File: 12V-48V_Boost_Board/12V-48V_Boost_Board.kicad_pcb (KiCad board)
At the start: 2 copper layers, 31 parts, among them J1 12V Input, J2 Input Current Sensing, J3 Output Current Sensing, J4 48V Output, Q1 100V

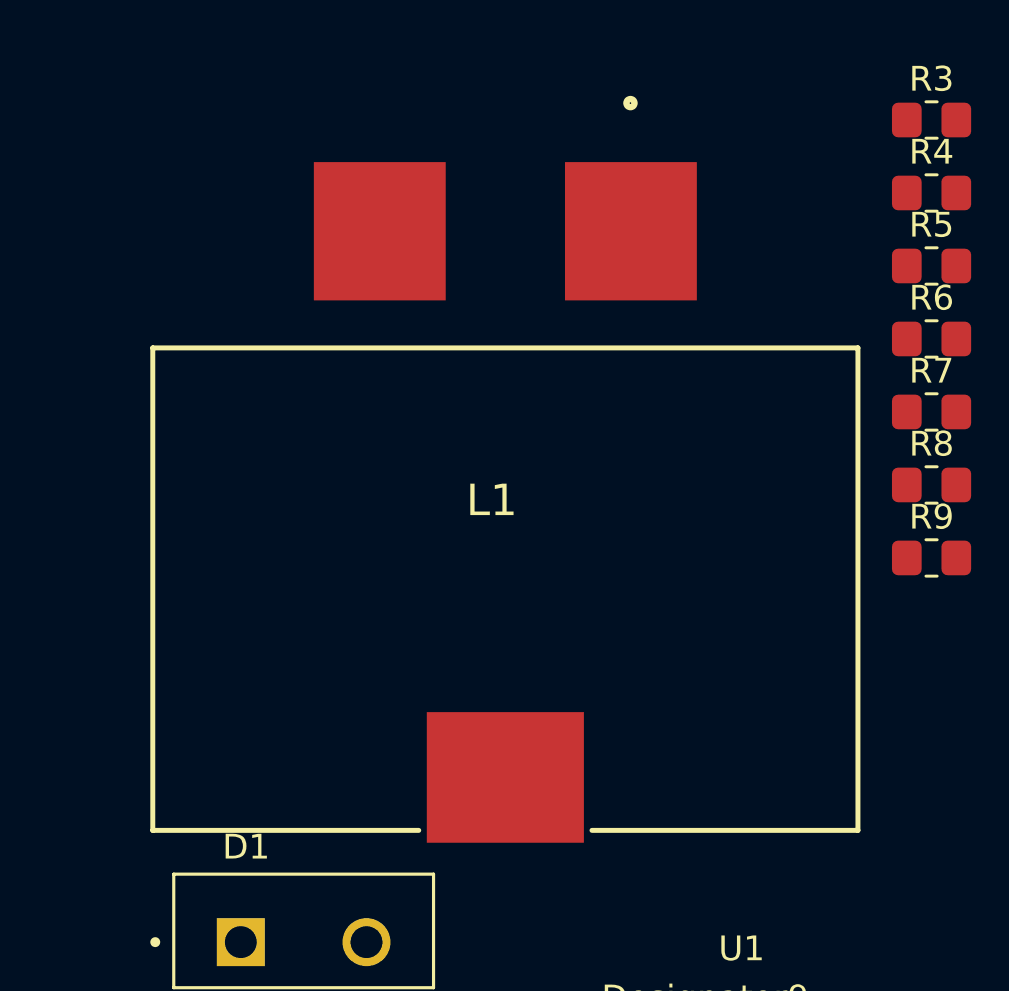
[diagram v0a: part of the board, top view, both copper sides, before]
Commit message: Implemented feedback from request V2
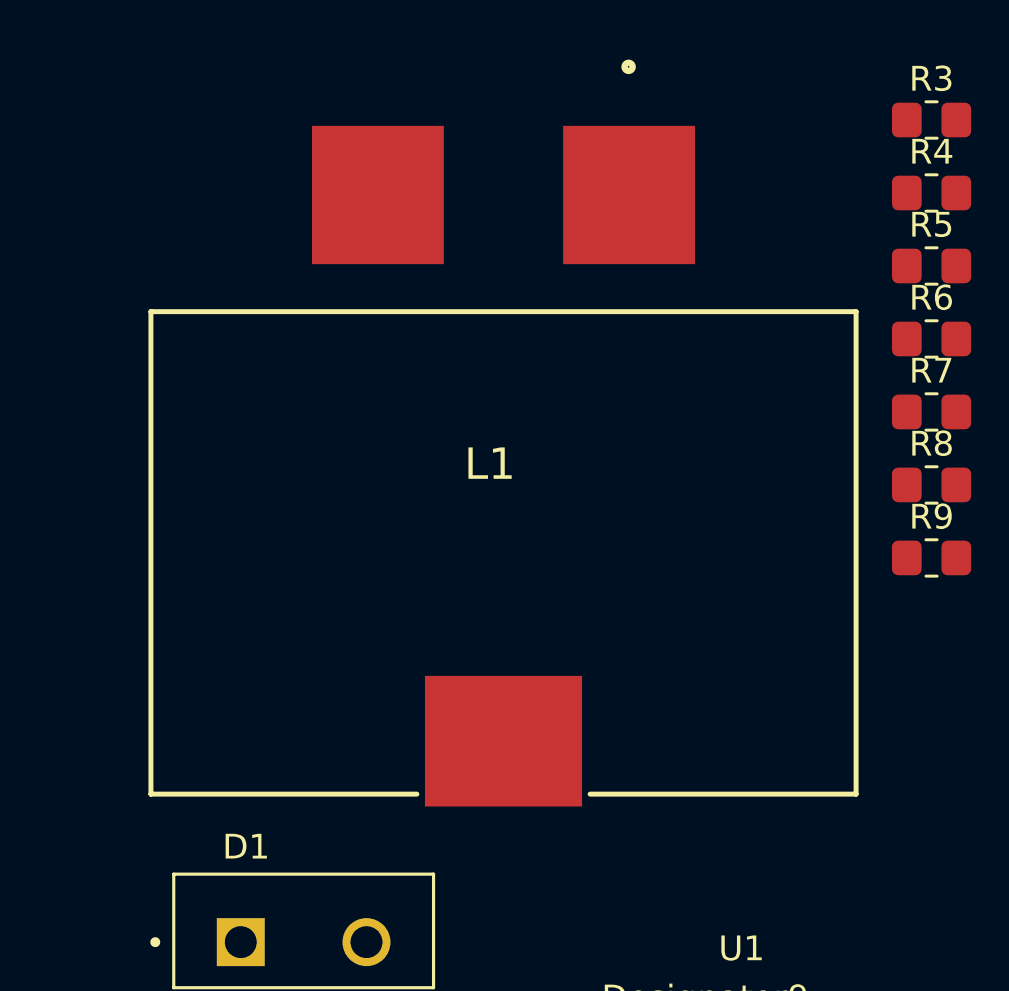
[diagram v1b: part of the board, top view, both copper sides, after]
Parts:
- moved L1 1.47 mm to (151.0, 107.0)
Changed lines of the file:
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@@
 	(footprint "Library:WE-HCF_SMD_HIGH-CURRENT_INDUCTOR"
 		(layer "F.Cu")
-		(at 151.075 108.465)
+		(at 151 107)
 		(descr "WE-HCF_SMD_High-Current_Inductor")
 		(tags "Inductor")

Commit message: First attempt in the pcb layout and routing
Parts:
- added C12: 1µF, Capacitor_SMD:C_0805_2012Metric_Pad1.18x1.45mm_HandSolder, F.Cu at (136.5, 128.0)
- added DNP1: 1mΩ, Resistor_SMD:R_0805_2012Metric_Pad1.20x1.40mm_HandSolder, F.Cu at (125.5, 100.5)
- added DNP2: ~, Resistor_SMD:R_0805_2012Metric_Pad1.20x1.40mm_HandSolder, F.Cu at (125.5, 93.5)
- added J5: Output Measuring, TerminalBlock_Phoenix:TerminalBlock_Phoenix_PT-1,5-2-5.0-H_1x02_P5.00mm_Horizontal, F.Cu at (117.0, 96.5)
- C11: value 1µF -> 10µF
- C2: value 100nF -> 4.7µF
- C3: value 63nF -> 100nF
- C4: value 1µF -> 63nF
- C5: value 120nF -> 1µF
- C6: value 100nF -> 120nF
- C7: value 1nF -> 100nF
- C8: value 10µF -> 1nF
- D1: value 800mV -> 455mV; footprint Library:TO-220-2 -> 12/48 boost:D2PAK_STM-M
- F1: footprint Fuse:Fuse_0805_2012Metric_Pad1.15x1.40mm_HandSolder -> Fuse:Fuse_1206_3216Metric
- F2: value 3A -> 2A; footprint Fuse:Fuse_0805_2012Metric_Pad1.15x1.40mm_HandSolder -> Fuse:Fuse_1206_3216Metric
- L1: footprint Library:WE-HCF_SMD_HIGH-CURRENT_INDUCTOR -> 12/48 boost:WE-HCF_SMD_HIGH-CURRENT_INDUCTOR
- Q1: value 100V -> FDWS86068-F085; footprint Library:Q1 Mosfet -> 12/48 boost:Q1 Mosfet
- TH1: footprint Library:Inrush Current Limiter -> 12/48 boost:Inrush Current Limiter
- U1: footprint Library:LM5156H -> 12/48 boost:LM5156H
- moved F1 78.4 mm to (194.0, 81.2), turned to -90 degrees
- moved J2 76.3 mm to (179.0, 78.5)
- moved TH1 66.3 mm to (187.5, 91.2), turned to -90 degrees
- moved R1 65.7 mm to (180.5, 86.0)
- moved J1 61.1 mm to (166.5, 78.5)
- moved C11 51.4 mm to (136.5, 132.0), turned to 180 degrees
- moved C10 49.4 mm to (141.5, 132.0), turned to 180 degrees
- moved C8 49.2 mm to (130.5, 105.5), turned to 180 degrees
- moved C9 48.8 mm to (141.5, 128.0), turned to 180 degrees
- moved R7 40.4 mm to (130.5, 115.5), turned to 180 degrees
- moved R6 39.7 mm to (130.5, 110.5)
- moved L1 39.1 mm to (188.5, 118.0), turned to 90 degrees
- moved U1 38.1 mm to (148.5, 94.0)
- moved C5 38.1 mm to (137.5, 88.0), turned to 180 degrees
- moved R4 35.6 mm to (136.5, 108.5), turned to 180 degrees
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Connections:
- C10 pad 1: Net-(C10-Pad1) -> /Boost_Board_Chip/48V_OUTPUT
- C3 pad 1: Net-(U1-SS) -> /Boost_Board_Chip/12V_INPUT
- C4 pad 1: /Boost_Board_Chip/DITHOFF -> Net-(U1-SS)
- C5 pad 1: Net-(U1-COMP) -> /Boost_Board_Chip/DITHOFF
- C6 pad 2: Net-(C6-Pad2) -> GND
- C7 pad 1: Net-(C7-Pad1) -> Net-(U1-COMP)
- C7 pad 2: GND -> Net-(C7-Pad2)
- C8 pad 1: /Boost_Board_Chip/48V_OUTPUT -> Net-(C8-Pad1)
- C8 pad 2: Net-(C8-Pad2) -> GND
- C9 pad 1: Net-(C8-Pad2) -> /Boost_Board_Chip/48V_OUTPUT
- C9 pad 2: Net-(C10-Pad1) -> GND
- J4 pad 2: GND -> Net-(J4-Pin_2)
- Q1 pad 2: Net-(Q1-G) -> Net-(Q1-S)
- Q1 pad 3: Net-(Q1-S) -> Net-(Q1-G)
- R4 pad 2: Net-(C7-Pad1) -> Net-(C8-Pad1)
- R5 pad 1: Net-(C6-Pad2) -> Net-(C7-Pad2)
- R6 pad 2: Net-(C7-Pad1) -> Net-(C8-Pad1)
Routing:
- net GND: track 0.00 -> 74.0 mm, vias 0 -> 4
- net /Boost_Board_Chip/12V_INPUT: track 0.00 -> 72.7 mm
- net /Boost_Board_Chip/48V_OUTPUT: track 0.00 -> 61.3 mm
- net Net-(Q1-G): track 0.00 -> 40.3 mm, vias 0 -> 2
- net Net-(Q1-S): track 0.00 -> 40.2 mm, vias 0 -> 2
- net /Boost_Board_Chip/DITHOFF: track 0.00 -> 32.0 mm, vias 0 -> 2
- net Net-(U1-FB): track 0.00 -> 30.9 mm
- net Net-(J3-Pin_1): track 0.00 -> 28.2 mm
- net Net-(D1-A): track 0.00 -> 25.4 mm
- net Net-(J2-Pin_2): track 0.00 -> 23.6 mm
- net Net-(J3-Pin_2): track 0.00 -> 21.3 mm
- net Net-(U1-COMP): track 0.00 -> 19.1 mm
- net Net-(U1-CS): track 0.00 -> 15.9 mm
- net Net-(J1-Pin_2): track 0.00 -> 15.2 mm
- net Net-(J5-Pin_1): track 0.00 -> 14.3 mm
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- added copper zone on B.Cu, net GND
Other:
- board outline added: 90 x 64 mm

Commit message: Made all the changes, still working on the refining the track sizes
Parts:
- removed DNP1: 1mΩ, Resistor_SMD:R_0805_2012Metric_Pad1.20x1.40mm_HandSolder
- removed DNP2: ~, Resistor_SMD:R_0805_2012Metric_Pad1.20x1.40mm_HandSolder
- added R3: DNP, Resistor_SMD:R_0805_2012Metric_Pad1.20x1.40mm_HandSolder, F.Cu at (125.5, 100.5)
- added R4: DNP, Resistor_SMD:R_0805_2012Metric_Pad1.20x1.40mm_HandSolder, F.Cu at (125.5, 93.5)
- moved TH1 4.92 mm to (192.4, 90.8)
- moved F1 2.21 mm to (194.0, 83.4)
- turned R8 to 180 degrees
- renumbered R8 to R10, R9 to R11, R3 to R5, R4 to R6, R5 to R7, R6 to R8, R7 to R9
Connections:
- J4 pad 2: Net-(J4-Pin_2) -> unconnected-(J4-Pin_2-Pad2)
- Q1 pad 2: Net-(Q1-S) -> (no net)
- Q1 pad 3: Net-(Q1-G) -> (no net)
- Q1 pad 4: (no net) -> Net-(Q1-G)
- Q1 pad 5: (no net) -> Net-(Q1-S)
- R8 pad 1: Net-(Q1-S) -> Net-(C8-Pad1)
- R8 pad 2: Net-(C8-Pad1) -> Net-(Q1-S)
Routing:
- net Net-(J3-Pin_2): track 21.3 -> 33.8 mm
- net Net-(J4-Pin_2): track 10.2 -> 0.00 mm
- net Net-(Q1-S): track 40.2 -> 33.2 mm
- net /Boost_Board_Chip/12V_INPUT: track 72.7 -> 77.8 mm
- net Net-(F1-Pad2): track 11.3 -> 6.72 mm
- net Net-(J2-Pin_2): track 23.6 -> 21.7 mm
- net GND: track 74.0 -> 74.7 mm
- added copper zone on F.Cu, net GND

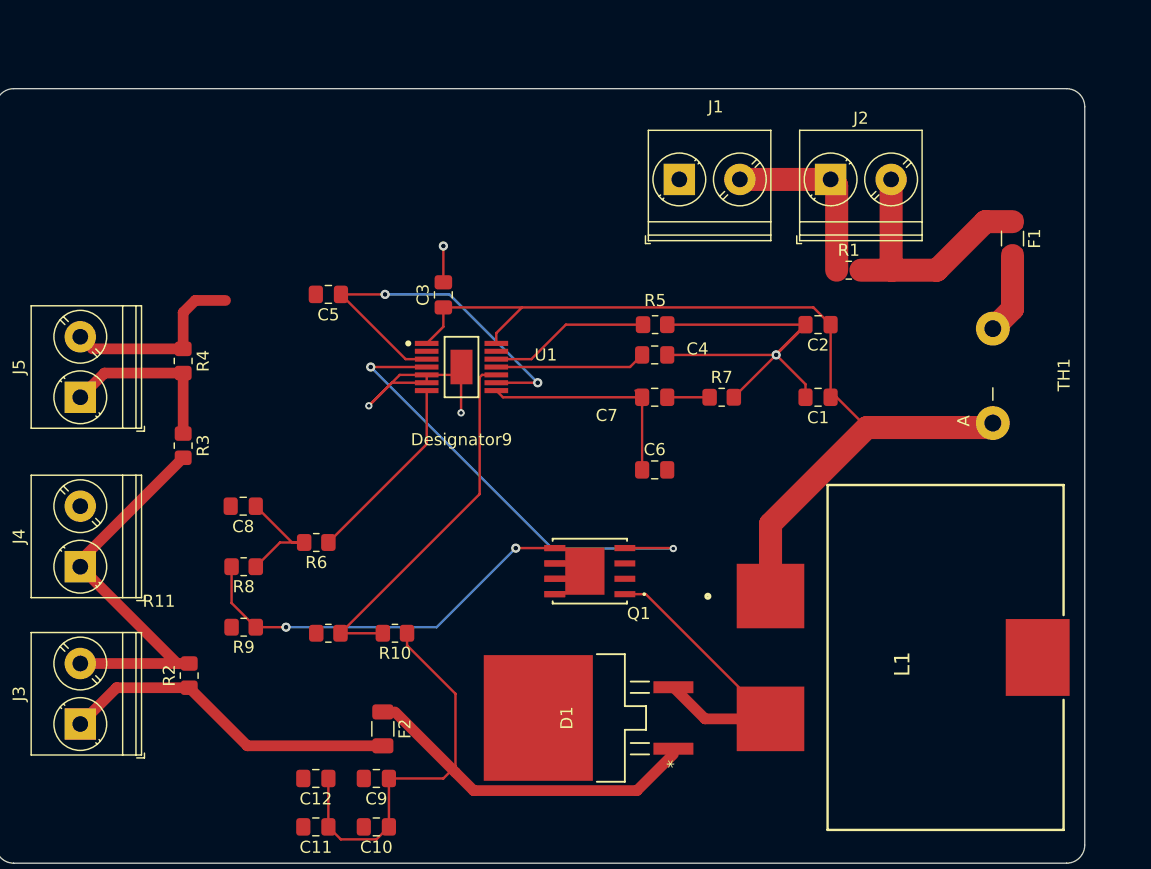
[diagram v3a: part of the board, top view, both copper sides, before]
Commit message: Made some changes to track sizes
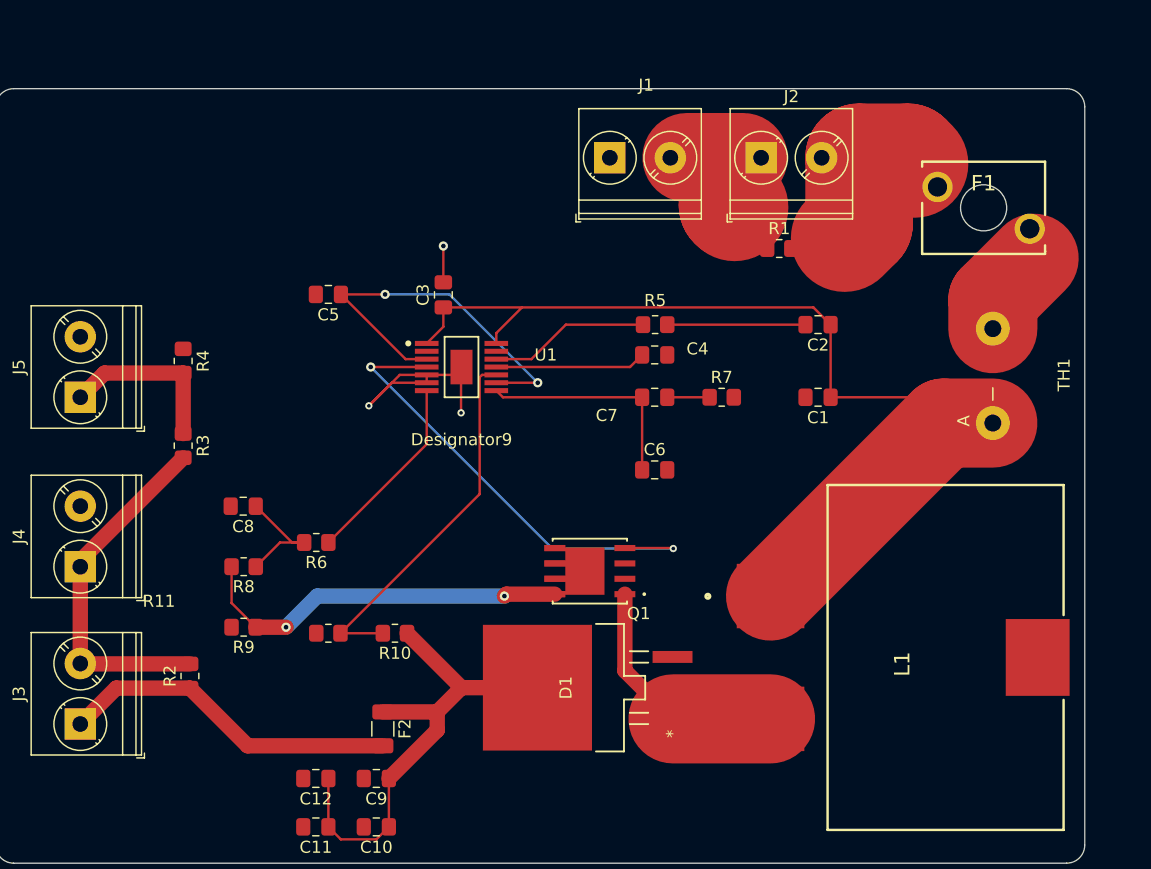
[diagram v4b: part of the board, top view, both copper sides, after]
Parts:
- F1: footprint Fuse:Fuse_1206_3216Metric -> 12/48 boost:01530009Z
- moved F1 7.53 mm to (187.8, 79.1), turned to 0 degrees
- moved J1 6.02 mm to (160.8, 76.7)
- moved J2 6.02 mm to (173.3, 76.7)
- moved R1 6.02 mm to (174.8, 84.2)
- moved D1 2.50 mm to (157.1, 120.5)
- moved R2 0.07 mm to (126.1, 119.5)
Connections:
- D1 pad 1: /Boost_Board_Chip/48V_OUTPUT -> Net-(D1-A)
- D1 pad 2: Net-(D1-A) -> (no net)
- D1 pad 3: (no net) -> /Boost_Board_Chip/48V_OUTPUT
- J4 pad 2: unconnected-(J4-Pin_2-Pad2) -> GND
- Q1 pad 5: Net-(Q1-S) -> (no net)
- Q1 pad 8: (no net) -> Net-(Q1-S)
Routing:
- net GND: track 74.7 -> 32.5 mm, vias 4 -> 3
- net /Boost_Board_Chip/48V_OUTPUT: track 61.3 -> 41.0 mm
- net Net-(J1-Pin_2): track 15.2 -> 4.95 mm
- net Net-(J2-Pin_2): track 21.7 -> 12.0 mm
- net Net-(D1-A): track 25.4 -> 20.0 mm
- net Net-(J3-Pin_2): track 33.8 -> 29.0 mm
- net /Boost_Board_Chip/12V_INPUT: track 77.8 -> 80.5 mm
- net Net-(Q1-S): track 33.2 -> 31.7 mm
- net Net-(U1-COMP): track 19.1 -> 18.3 mm
- net Net-(F1-Pad2): track 6.72 -> 7.23 mm

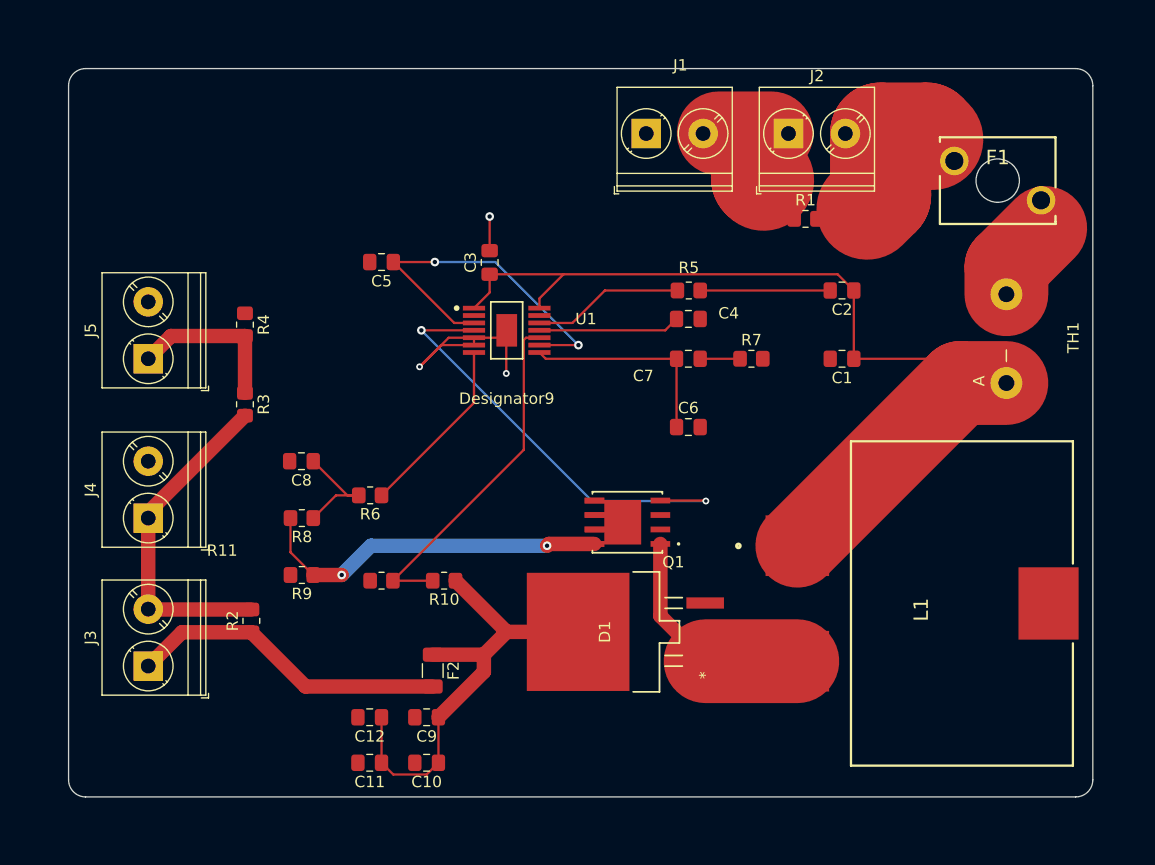
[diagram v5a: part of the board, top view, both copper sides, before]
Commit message: Squeezed board closer and rerouted traces
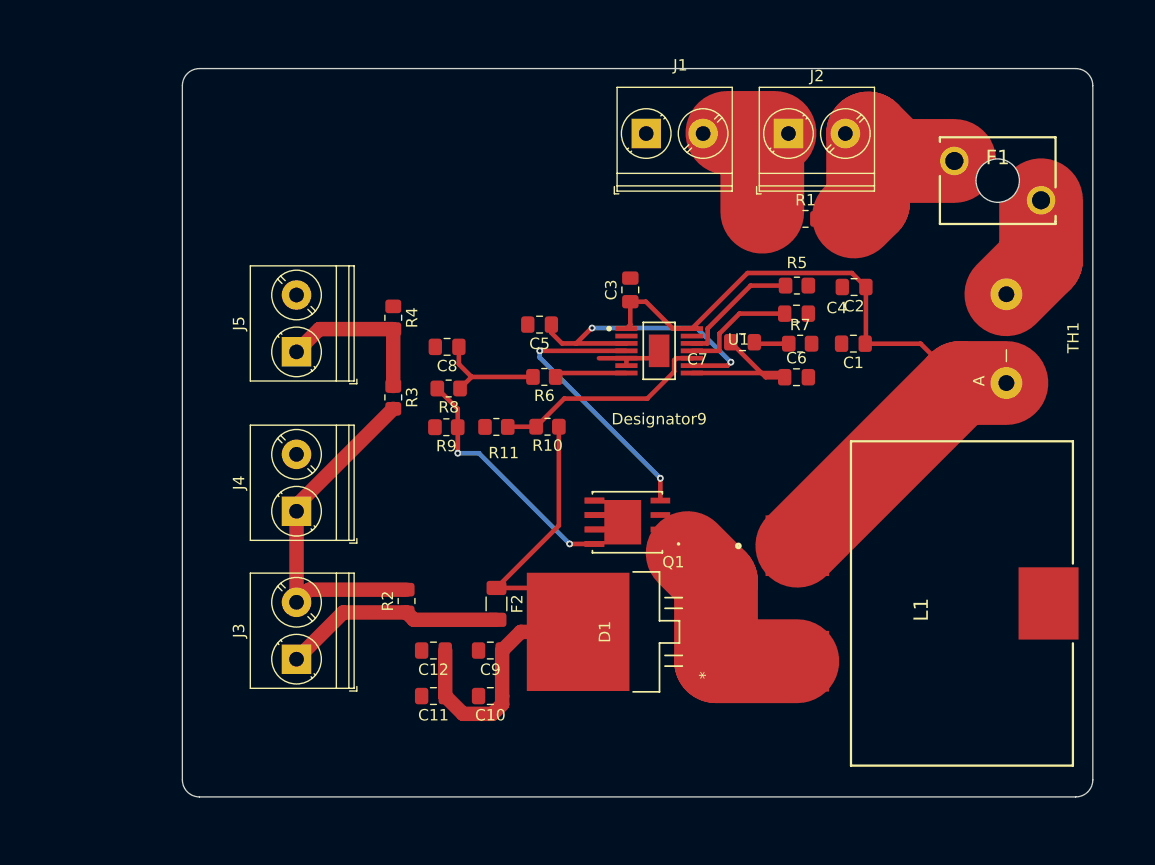
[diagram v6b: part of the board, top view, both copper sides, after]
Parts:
- moved R6 18.5 mm to (151.8, 98.1)
- moved R9 18.2 mm to (143.2, 102.5)
- moved R8 17.2 mm to (143.4, 99.1)
- moved R11 16.9 mm to (147.6, 102.5)
- moved R10 16.3 mm to (152.1, 102.5)
- moved C8 16.3 mm to (143.3, 95.5)
- moved C5 14.9 mm to (151.4, 93.5)
- moved R2 13.8 mm to (139.7, 117.8)
- moved U1 13.5 mm to (161.9, 95.8)
- moved J3 13.0 mm to (130.0, 122.9)
- moved J4 13.0 mm to (130.0, 109.9)
- moved J5 13.0 mm to (130.0, 95.9)
- moved R3 13.0 mm to (138.5, 99.9)
- moved R4 13.0 mm to (138.5, 92.9)
- moved C3 12.6 mm to (159.4, 90.4)
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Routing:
- net GND: track 32.5 -> 5.29 mm, vias 3 -> 0
- net /Boost_Board_Chip/12V_INPUT: track 80.5 -> 65.7 mm
- net Net-(Q1-G): track 39.9 -> 25.2 mm
- net Net-(U1-FB): track 30.9 -> 19.2 mm
- net Net-(U1-CS): track 15.9 -> 5.87 mm
- net Net-(Q1-S): track 31.7 -> 21.7 mm
- net Net-(J3-Pin_1): track 28.2 -> 19.5 mm
- net /Boost_Board_Chip/DITHOFF: track 32.0 -> 26.7 mm
- net Net-(U1-COMP): track 18.3 -> 13.8 mm
- net Net-(J2-Pin_2): track 12.0 -> 16.4 mm
- net Net-(J1-Pin_2): track 4.95 -> 8.28 mm
- net Net-(D1-A): track 20.0 -> 17.7 mm
- net Net-(F1-Pad2): track 7.23 -> 9.52 mm
- net Net-(U1-RT): track 13.3 -> 11.1 mm
- net Net-(U1-SS): track 12.5 -> 10.4 mm
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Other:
- board size 90 x 64 mm -> 80 x 64 mm
